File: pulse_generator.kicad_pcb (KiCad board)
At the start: 2 copper layers, 82.6 x 55.9 mm, 10 parts, among them J1 Power, J2 Digital/PWM, J3 Analog, J4 Digital/PWM, J5 Conn_Coaxial, J6 Conn_Coaxial

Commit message: sch rev2
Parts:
- added C1: 100n, Capacitor_SMD:C_0805_2012Metric_Pad1.18x1.45mm_HandSolder, F.Cu at (157.2, 65.7)
- added C3: 100n, Capacitor_SMD:C_0805_2012Metric_Pad1.18x1.45mm_HandSolder, F.Cu at (141.9, 81.0)
- added D1: 1N5711, Diode_SMD:D_SOD-123, F.Cu at (145.7, 93.7)
- added D2: 1N5711, Diode_SMD:D_SOD-123, F.Cu at (155.9, 93.7)
- added D3: LED, LED_THT:LED_D5.0mm, F.Cu at (205.7, 71.1)
- added R1: 1M, Resistor_SMD:R_0805_2012Metric_Pad1.20x1.40mm_HandSolder, F.Cu at (150.8, 92.7)
- added R2: 1M, Resistor_SMD:R_0805_2012Metric_Pad1.20x1.40mm_HandSolder, F.Cu at (121.6, 82.0)
- added R3: 10k, Resistor_SMD:R_0805_2012Metric_Pad1.20x1.40mm_HandSolder, F.Cu at (146.7, 77.1)
- added R4: 330, Resistor_SMD:R_0805_2012Metric_Pad1.20x1.40mm_HandSolder, F.Cu at (121.6, 63.4)
- added U1: LM311, Package_DIP:DIP-8_W7.62mm_LongPads, F.Cu at (145.7, 88.6)
- added U2: 74LS279, Package_DIP:DIP-16_W7.62mm_LongPads, F.Cu at (153.3, 58.1)
- moved J5 16.5 mm to (112.7, 81.0)
- moved J6 16.5 mm to (112.7, 64.4)
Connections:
- J2 pad 1: /SCL/A5 -> unconnected-(J2-Pad1)
- J2 pad 2: /SDA/A4 -> unconnected-(J2-Pad2)
- J3 pad 5: /SDA/A4 -> unconnected-(J3-Pad5)
- J3 pad 6: /SCL/A5 -> unconnected-(J3-Pad6)
- J5 pad 1: unconnected-(J5-Pad1) -> Net-(J5-Pad1)
- J5 pad 2: unconnected-(J5-Pad2) -> GND
- J6 pad 1: unconnected-(J6-Pad1) -> Net-(J6-Pad1)
- J6 pad 2: unconnected-(J6-Pad2) -> GND
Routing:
- added copper zone on In2.Cu, net +5V
- added copper zone on In1.Cu, net GND
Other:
- board size 82.6 x 55.9 mm -> 82.6 x 54.6 mm
- copper layers 2 -> 4

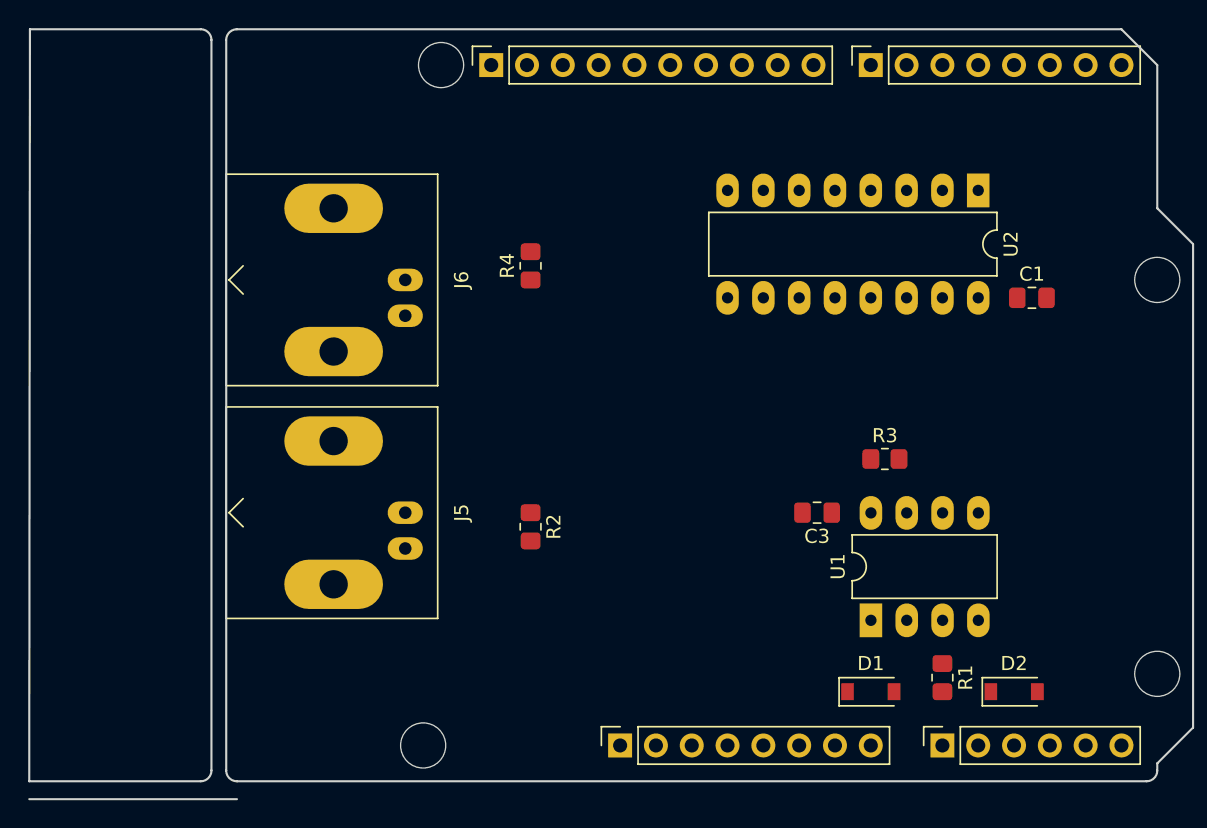
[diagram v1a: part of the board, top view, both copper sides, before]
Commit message: guardat amb og shield outline
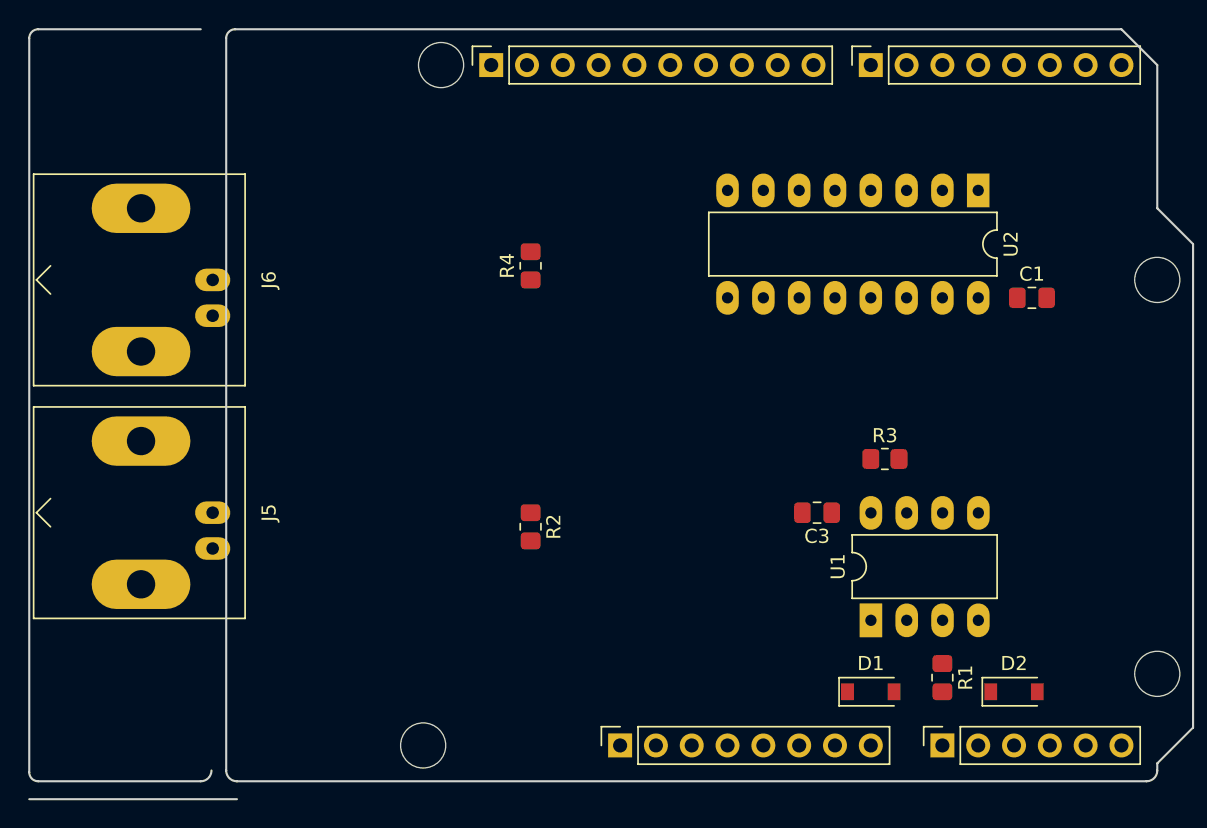
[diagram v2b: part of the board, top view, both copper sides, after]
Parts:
- moved J5 13.7 mm to (99.0, 81.0)
- moved J6 13.7 mm to (99.0, 64.4)
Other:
- outline, holes or cut-outs redrawn
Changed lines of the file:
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@@
   )
   (footprint "Connector_Coaxial:BNC_Amphenol_B6252HB-NPP3G-50_Horizontal" (layer "F.Cu")
-    (at 112.7 80.95 90)
+    (at 99.04 80.95 90)
     (descr "http://www.farnell.com/datasheets/612848.pdf")
     (tags "BNC Amphenol Horizontal")
@@
   )
   (footprint "Connector_Coaxial:BNC_Amphenol_B6252HB-NPP3G-50_Horizontal" (layer "F.Cu")
-    (at 112.7 64.44 90)
+    (at 99.04 64.44 90)
     (descr "http://www.farnell.com/datasheets/612848.pdf")
     (tags "BNC Amphenol Horizontal")
@@
   (gr_line (start 109.525 67.615) (end 93.65 67.615) (layer "Dwgs.User") (width 0.15))
   (gr_arc (start 98.953185 99.238) (mid 98.73 99.776815) (end 98.191185 100) (layer "Edge.Cuts") (width 0.15))
-  (gr_line (start 86.08 46.66) (end 86.03 100) (layer "Edge.Cuts") (width 0.15))
+  (gr_line (start 86.03 47.295) (end 86.03 99.365) (layer "Edge.Cuts") (width 0.15))
   (gr_line (start 166.04 59.36) (end 168.58 61.9) (layer "Edge.Cuts") (width 0.15))
-  (gr_line (start 100 99.238) (end 100 47.422) (layer "Edge.Cuts") (width 0.15))
-  (gr_line (start 98.191185 46.66) (end 86.08 46.66) (layer "Edge.Cuts") (width 0.15))
+  (gr_line (start 100 47.295) (end 100 99.238) (layer "Edge.Cuts") (width 0.15))
+  (gr_line (start 98.191185 46.66) (end 86.665 46.66) (layer "Edge.Cuts") (width 0.15))
   (gr_line (start 86.03 101.27) (end 100.762 101.27) (layer "Edge.Cuts") (width 0.15))
   (gr_line (start 168.58 61.9) (end 168.58 96.19) (layer "Edge.Cuts") (width 0.15))
   (gr_line (start 165.278 100) (end 100.762 100) (layer "Edge.Cuts") (width 0.15))
-  (gr_line (start 100.762 46.66) (end 163.5 46.66) (layer "Edge.Cuts") (width 0.15))
+  (gr_arc (start 86.665 100) (mid 86.215987 99.814013) (end 86.03 99.365) (layer "Edge.Cuts") (width 0.15))
+  (gr_line (start 100.635 46.66) (end 163.5 46.66) (layer "Edge.Cuts") (width 0.15))
   (gr_arc (start 100.762 100) (mid 100.223185 99.776815) (end 100 99.238) (layer "Edge.Cuts") (width 0.15))
+  (gr_arc (start 100 47.295) (mid 100.185987 46.845987) (end 100.635 46.66) (layer "Edge.Cuts") (width 0.15))
   (gr_line (start 168.58 96.19) (end 166.04 98.73) (layer "Edge.Cuts") (width 0.15))
-  (gr_line (start 98.953185 47.422) (end 98.953185 99.238) (layer "Edge.Cuts") (width 0.15))
-  (gr_arc (start 98.191185 46.66) (mid 98.73 46.883185) (end 98.953185 47.422) (layer "Edge.Cuts") (width 0.15))
   (gr_line (start 163.5 46.66) (end 166.04 49.2) (layer "Edge.Cuts") (width 0.15))
-  (gr_line (start 86.03 100) (end 98.191185 100) (layer "Edge.Cuts") (width 0.15))
+  (gr_line (start 86.665 100) (end 98.191185 100) (layer "Edge.Cuts") (width 0.15))
   (gr_arc (start 166.04 99.238) (mid 165.816815 99.776815) (end 165.278 100) (layer "Edge.Cuts") (width 0.15))
+  (gr_arc (start 86.03 47.295) (mid 86.215987 46.845987) (end 86.665 46.66) (layer "Edge.Cuts") (width 0.15))
   (gr_line (start 166.04 49.2) (end 166.04 59.36) (layer "Edge.Cuts") (width 0.15))
   (gr_line (start 166.04 98.73) (end 166.04 99.238) (layer "Edge.Cuts") (width 0.15))
-  (gr_arc (start 100 47.422) (mid 100.223185 46.883185) (end 100.762 46.66) (layer "Edge.Cuts") (width 0.15))
   (gr_text "ICSP" (at 164.897 72.06 90) (layer "Dwgs.User")
     (effects (font (size 1 1) (thickness 0.15)))

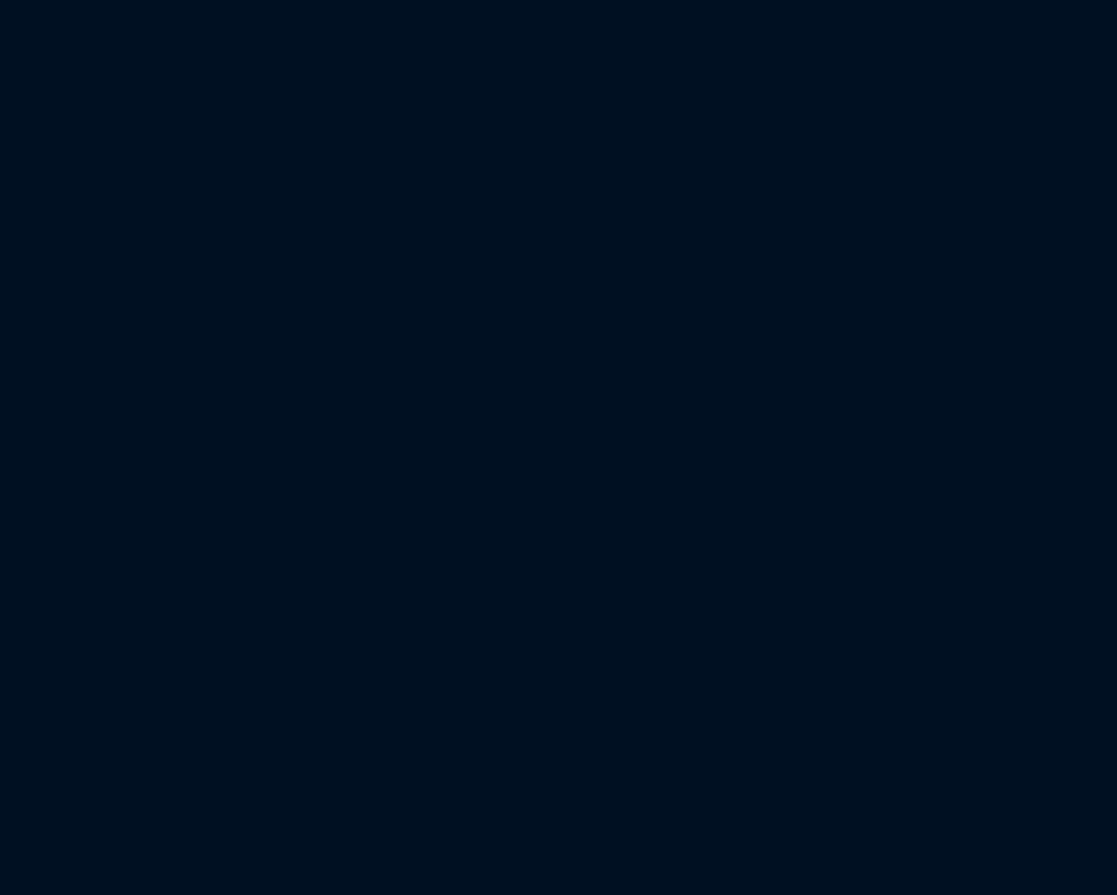
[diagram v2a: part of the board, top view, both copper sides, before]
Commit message: shield edge cuts save
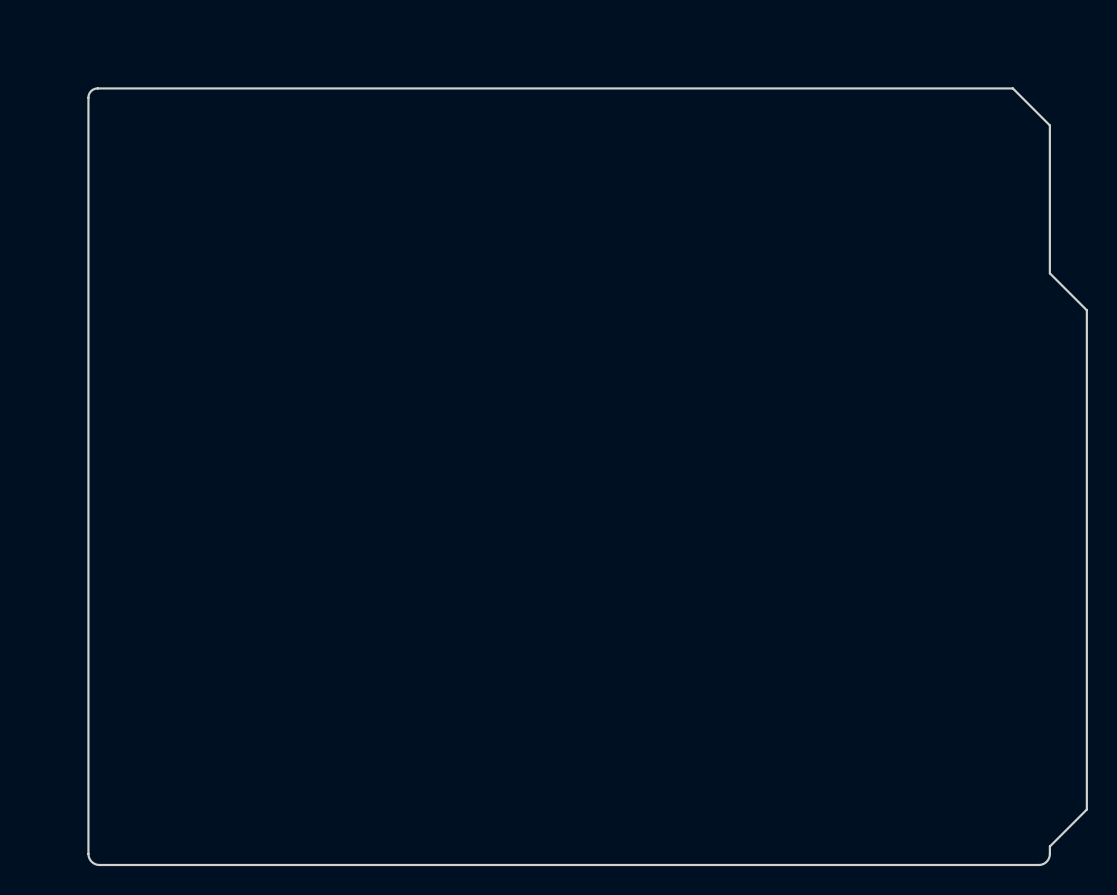
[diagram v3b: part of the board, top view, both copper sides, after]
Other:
- board size 82.6 x 54.6 mm -> 186.3 x 109.4 mm
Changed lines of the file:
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@@
   (gr_line (start 168.58 45.39) (end 86.08 45.39) (layer "Dwgs.User") (width 0.15))
   (gr_line (start 109.525 67.615) (end 93.65 67.615) (layer "Dwgs.User") (width 0.15))
+  (gr_line (start 204.363185 102.763185) (end 267.228185 102.763185) (layer "Edge.Cuts") (width 0.15))
   (gr_arc (start 98.953185 99.238) (mid 98.73 99.776815) (end 98.191185 100) (layer "Edge.Cuts") (width 0.15))
   (gr_line (start 86.03 47.295) (end 86.03 99.365) (layer "Edge.Cuts") (width 0.15))
+  (gr_arc (start 269.768185 155.341185) (mid 269.545 155.88) (end 269.006185 156.103185) (layer "Edge.Cuts") (width 0.15))
   (gr_line (start 166.04 59.36) (end 168.58 61.9) (layer "Edge.Cuts") (width 0.15))
+  (gr_line (start 272.308185 152.293185) (end 269.768185 154.833185) (layer "Edge.Cuts") (width 0.15))
+  (gr_line (start 272.308185 118.003185) (end 272.308185 152.293185) (layer "Edge.Cuts") (width 0.15))
   (gr_line (start 100 47.295) (end 100 99.238) (layer "Edge.Cuts") (width 0.15))
   (gr_line (start 98.191185 46.66) (end 86.665 46.66) (layer "Edge.Cuts") (width 0.15))
   (gr_line (start 86.03 101.27) (end 100.762 101.27) (layer "Edge.Cuts") (width 0.15))
   (gr_line (start 168.58 61.9) (end 168.58 96.19) (layer "Edge.Cuts") (width 0.15))
+  (gr_line (start 269.768185 105.303185) (end 269.768185 115.463185) (layer "Edge.Cuts") (width 0.15))
   (gr_line (start 165.278 100) (end 100.762 100) (layer "Edge.Cuts") (width 0.15))
   (gr_arc (start 86.665 100) (mid 86.215987 99.814013) (end 86.03 99.365) (layer "Edge.Cuts") (width 0.15))
   (gr_line (start 100.635 46.66) (end 163.5 46.66) (layer "Edge.Cuts") (width 0.15))
+  (gr_arc (start 203.728185 103.398185) (mid 203.914172 102.949172) (end 204.363185 102.763185) (layer "Edge.Cuts") (width 0.15))
   (gr_arc (start 100.762 100) (mid 100.223185 99.776815) (end 100 99.238) (layer "Edge.Cuts") (width 0.15))
+  (gr_line (start 203.728185 103.398185) (end 203.728185 155.341185) (layer "Edge.Cuts") (width 0.15))
   (gr_arc (start 100 47.295) (mid 100.185987 46.845987) (end 100.635 46.66) (layer "Edge.Cuts") (width 0.15))
   (gr_line (start 168.58 96.19) (end 166.04 98.73) (layer "Edge.Cuts") (width 0.15))
+  (gr_line (start 267.228185 102.763185) (end 269.768185 105.303185) (layer "Edge.Cuts") (width 0.15))
   (gr_line (start 163.5 46.66) (end 166.04 49.2) (layer "Edge.Cuts") (width 0.15))
   (gr_line (start 86.665 100) (end 98.191185 100) (layer "Edge.Cuts") (width 0.15))
   (gr_arc (start 166.04 99.238) (mid 165.816815 99.776815) (end 165.278 100) (layer "Edge.Cuts") (width 0.15))
+  (gr_line (start 269.006185 156.103185) (end 204.490185 156.103185) (layer "Edge.Cuts") (width 0.15))
+  (gr_arc (start 204.490185 156.103185) (mid 203.95137 155.88) (end 203.728185 155.341185) (layer "Edge.Cuts") (width 0.15))
   (gr_arc (start 86.03 47.295) (mid 86.215987 46.845987) (end 86.665 46.66) (layer "Edge.Cuts") (width 0.15))
   (gr_line (start 166.04 49.2) (end 166.04 59.36) (layer "Edge.Cuts") (width 0.15))
   (gr_line (start 166.04 98.73) (end 166.04 99.238) (layer "Edge.Cuts") (width 0.15))
+  (gr_line (start 269.768185 115.463185) (end 272.308185 118.003185) (layer "Edge.Cuts") (width 0.15))
+  (gr_line (start 269.768185 154.833185) (end 269.768185 155.341185) (layer "Edge.Cuts") (width 0.15))
   (gr_text "ICSP" (at 164.897 72.06 90) (layer "Dwgs.User")
     (effects (font (size 1 1) (thickness 0.15)))

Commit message: nucleo form factor
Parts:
- moved D3 114.9 mm to (92.0, 54.8), turned to 90 degrees
- moved R2 35.2 mm to (156.0, 89.5)
- moved R4 16.7 mm to (105.5, 68.0)
- moved J5 10.1 mm to (99.0, 91.0)
- moved D1 5.08 mm to (150.8, 93.7)
- moved J6 4.56 mm to (99.0, 69.0)
- moved U1 4.54 mm to (148.3, 84.8)
- moved C3 4.54 mm to (144.4, 77.2)
- moved R3 4.05 mm to (149.3, 74.0)
- moved R1 4.05 mm to (153.3, 89.5)
- moved C1 2.60 mm to (159.7, 66.3)
- moved U2 2.60 mm to (155.9, 58.7)
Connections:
- D1 pad 2: /A0 -> /A2
- D2 pad 1: /A0 -> /A2
- R1 pad 2: /A0 -> /A2
- U1 pad 2: /A2 -> /A0
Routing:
- net Net-(J5-Pad1): track 0.00 -> 61.7 mm
- net Net-(J6-Pad1): track 0.00 -> 50.9 mm
- net Net-(D3-Pad2): track 0.00 -> 24.3 mm
- net /A0: track 0.00 -> 12.7 mm
- net /A2: track 0.00 -> 10.0 mm
- net GND: track 0.00 -> 1.50 mm, vias 0 -> 1
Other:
- outline, holes or cut-outs redrawn

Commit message: Ready for review
Ready for review
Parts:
- added D4: LED, LED_SMD:LED_0805_2012Metric_Pad1.15x1.40mm_HandSolder, F.Cu at (99.0, 76.0)
- added D5: LED, LED_SMD:LED_0805_2012Metric_Pad1.15x1.40mm_HandSolder, F.Cu at (94.0, 57.0)
- added R5: 10k, Resistor_SMD:R_0805_2012Metric_Pad1.20x1.40mm_HandSolder, F.Cu at (127.0, 72.0)
- added R6: 330, Resistor_SMD:R_0805_2012Metric_Pad1.20x1.40mm_HandSolder, F.Cu at (106.5, 60.0)
- added R7: 330, Resistor_SMD:R_0805_2012Metric_Pad1.20x1.40mm_HandSolder, F.Cu at (106.0, 76.0)
- added SW1: SW_Push, Button_Switch_THT:SW_Tactile_SPST_Angled_PTS645Vx39-2LFS, F.Cu at (90.2, 81.3)
- added TP1: GND_hook, Connector_PinHeader_2.54mm:PinHeader_1x01_P2.54mm_Vertical, F.Cu at (139.0, 84.5)
- added TP2: DAC_cal, Connector_PinHeader_2.54mm:PinHeader_1x01_P2.54mm_Vertical, F.Cu at (139.0, 91.5)
- J1, J4: footprint Connector_PinSocket_2.54mm:PinSocket_1x08_P2.54mm_Vertical -> Connector_PinHeader_2.54mm:PinHeader_1x08_P2.54mm_Vertical; moved to B.Cu
- J2: footprint Connector_PinSocket_2.54mm:PinSocket_1x10_P2.54mm_Vertical -> Connector_PinHeader_2.54mm:PinHeader_1x10_P2.54mm_Vertical; moved to B.Cu
- J3: footprint Connector_PinSocket_2.54mm:PinSocket_1x06_P2.54mm_Vertical -> Connector_PinHeader_2.54mm:PinHeader_1x06_P2.54mm_Vertical; moved to B.Cu
- U1: footprint Package_DIP:DIP-8_W7.62mm_LongPads -> Package_DIP:DIP-8_W7.62mm_Socket_LongPads
- U2: footprint Package_DIP:DIP-16_W7.62mm_LongPads -> Package_DIP:DIP-16_W7.62mm_Socket_LongPads
- moved U1 22.4 mm to (126.2, 88.6)
- moved R3 22.3 mm to (127.0, 74.5)
- moved C3 22.2 mm to (122.5, 80.8)
- moved R1 13.6 mm to (148.0, 77.0)
- moved R2 12.5 mm to (156.5, 77.0)
- moved C1 11.6 mm to (148.1, 66.0)
- moved U2 11.6 mm to (144.2, 58.4)
- moved D1 11.0 mm to (146.5, 83.5)
- moved D2 10.5 mm to (158.5, 83.5)
- moved R4 7.91 mm to (113.0, 65.5)
- moved J6 2.50 mm to (99.1, 66.5)
- moved D3 2.48 mm to (92.0, 52.3)
- moved J5 0.52 mm to (99.2, 91.5)
- turned J1 to -90 degrees
- turned J2 to -90 degrees
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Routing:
- net /~{RESET}: track 0.00 -> 60.1 mm
- net /2: track 0.00 -> 59.1 mm
- net /4: track 0.00 -> 30.6 mm
- net +3V3: track 0.00 -> 21.6 mm
- net /A2: track 10.0 -> 28.6 mm
- net +5V: track 0.00 -> 17.6 mm, vias 0 -> 2
- net /A0: track 12.7 -> 29.4 mm
- net Net-(D5-K): track 0.00 -> 12.9 mm
- net Net-(J6-In): track 50.9 -> 41.2 mm
- net GND: track 1.50 -> 11.0 mm, vias 1 -> 7
- net Net-(J5-In): track 61.7 -> 67.0 mm
- net Net-(D4-K): track 0.00 -> 4.97 mm
- net Net-(D3-A): track 24.3 -> 28.6 mm
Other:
- board size 186.3 x 109.4 mm -> 82.6 x 53 mm
- board text added: "(A0)"
- board text added: "1M"
- board text added: "1N5711"
- board text added: "3V3"
- board text added: "A2"
- board text added: "D1"
- board text added: "D2"
- board text added: "D3: Dialight 550-2407F or matching 5mm LED"
- board text added: "Electronics: D.Allepuz PCB: G.Allepuz"
- board text added: "Input"
- board text added: "J5"
- board text added: "J5/J6: Amphenol B6252H5-NPP3G-50 or matching BNC"
- board text added: "Mod friendly layout + part nums and values"
- board text added: "Output"
- board text added: "PULSED LASER ABLATOR PLL INTERFACE for use with SMT32 nucleo 64 series"
- board text added: "Pull-down"
- board text added: "Pull-up"
- board text added: "R1"
- board text added: "R2"
- board text added: "R6 & R7 (5V) set backlight brightness"
- board text added: "U1.3"
- board text added: "U1.7"
- board text added: "U1: LM311"
- board text added: "U2: 74LS279"
- board text added: "Your substrate never stood a chance"
- board text added: "github.com/gallepuz/laser-feedback"
- board text removed: "ICSP"
